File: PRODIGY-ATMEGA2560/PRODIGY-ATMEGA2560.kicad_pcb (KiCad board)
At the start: 4 copper layers, 22 parts, among them J1 DF40C-100DS-0.4V(51), J2 DF40C-100DS-0.4V(51), Q1 BC850, Q2 BC850, U1 ATmega2560-16A, U2 TXS0108EPW, U3 FT231XQ, Y1 16MHz

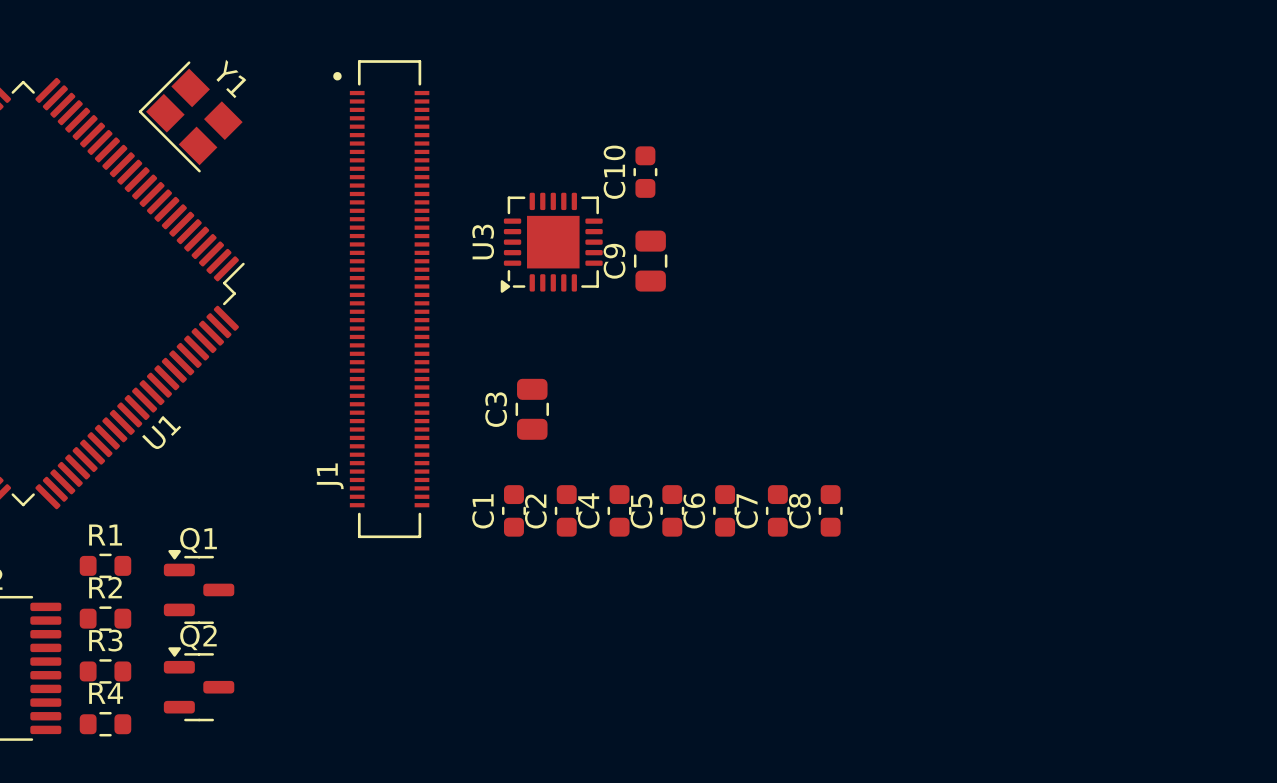
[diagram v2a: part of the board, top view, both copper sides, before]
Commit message: ESP32 and ATMEGA bom done.
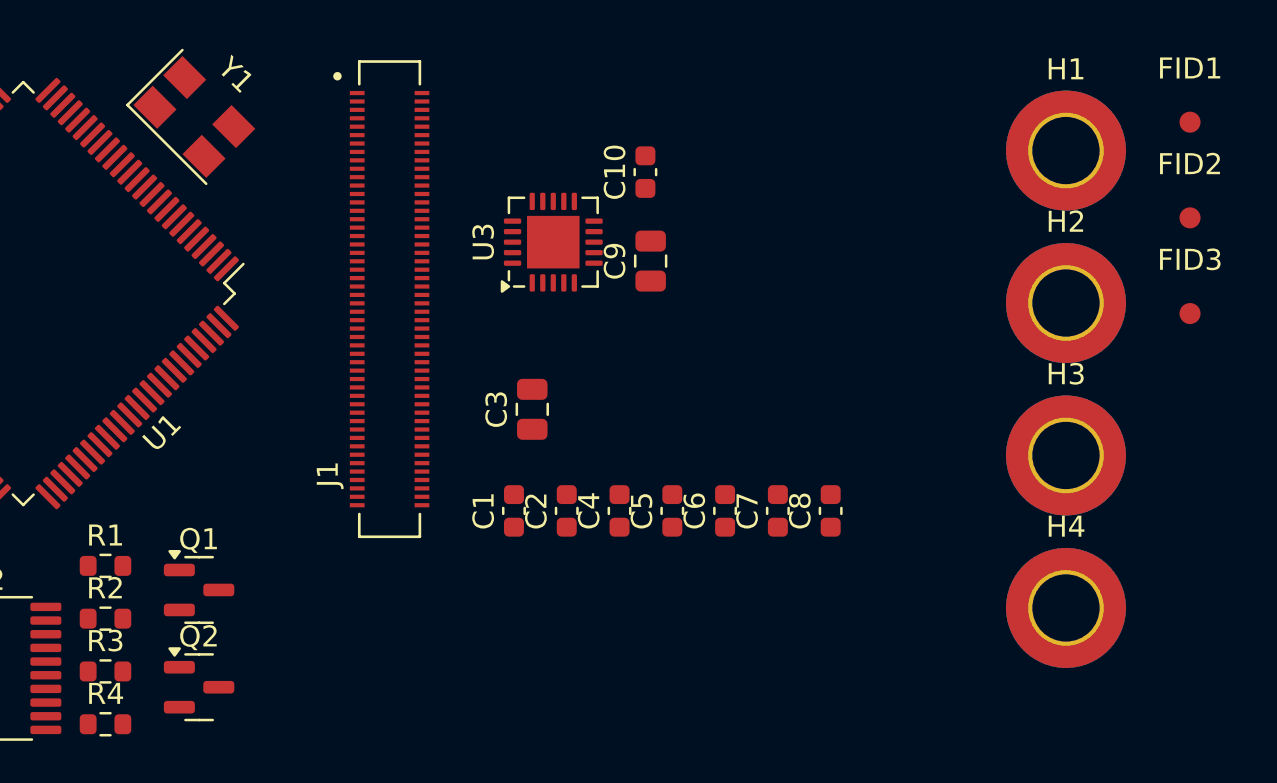
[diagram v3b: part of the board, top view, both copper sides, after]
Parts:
- added FID1: Fiducial, Fiducial:Fiducial_1mm_Mask3mm, F.Cu at (172.4, 64.9)
- added FID2: Fiducial, Fiducial:Fiducial_1mm_Mask3mm, F.Cu at (172.4, 69.5)
- added FID3: Fiducial, Fiducial:Fiducial_1mm_Mask3mm, F.Cu at (172.4, 74.0)
- added H1: MountingHole, MountingHole:MountingHole_3.2mm_M3_ISO7380_Pad_TopBottom, F.Cu at (166.5, 66.2)
- added H2: MountingHole, MountingHole:MountingHole_3.2mm_M3_ISO7380_Pad_TopBottom, F.Cu at (166.5, 73.5)
- added H3: MountingHole, MountingHole:MountingHole_3.2mm_M3_ISO7380_Pad_TopBottom, F.Cu at (166.5, 80.8)
- added H4: MountingHole, MountingHole:MountingHole_3.2mm_M3_ISO7380_Pad_TopBottom, F.Cu at (166.5, 88.0)
- C1, C2: value 10pF -> 4.7pF
- J1, J2: value DF40C-100DS-0.4V(51) -> DF40C-100DP-04V-51
- U1: value ATmega2560-16A -> ATmega2560-8A
- Y1: value 16MHz -> 8MHz; footprint Crystal:Crystal_SMD_3225-4Pin_3.2x2.5mm -> Crystal:Crystal_SMD_5032-4Pin_5.0x3.2mm

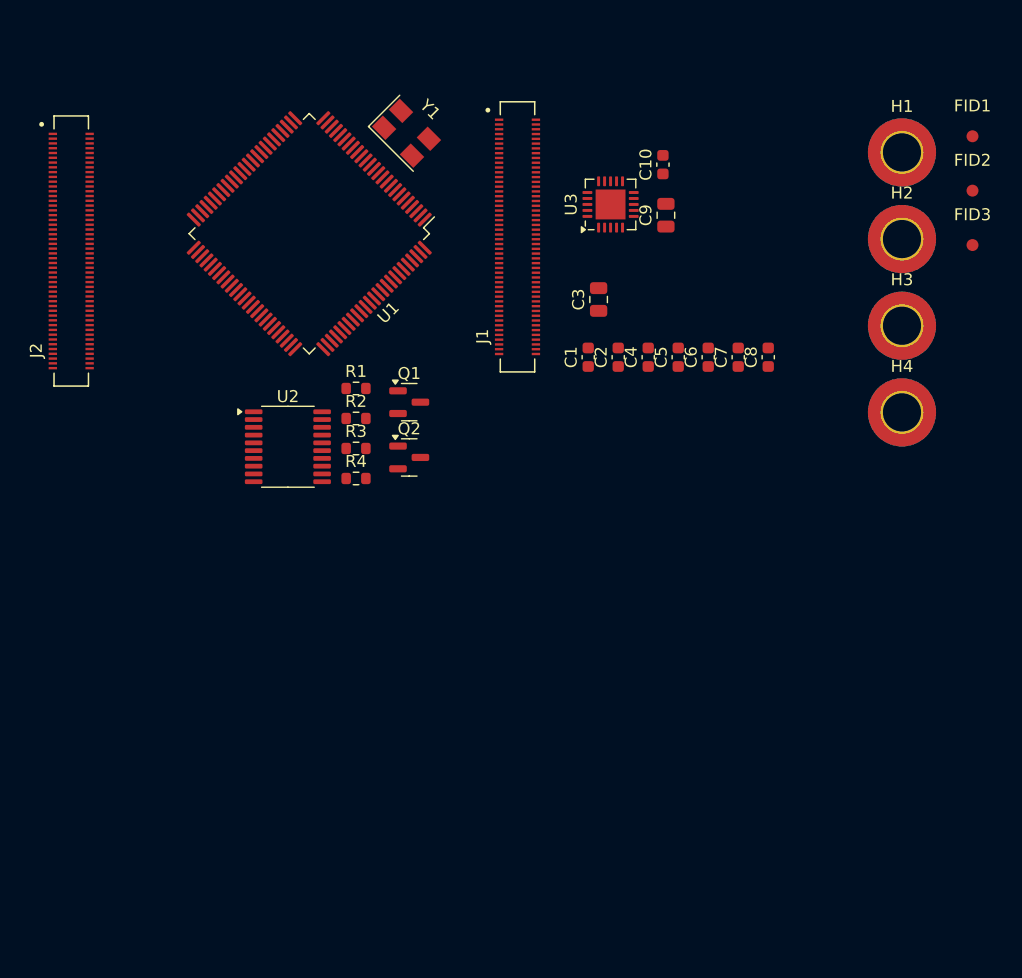
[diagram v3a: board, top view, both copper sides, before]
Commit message: Atmega layout done. orientation and alignment testing done. routing started.
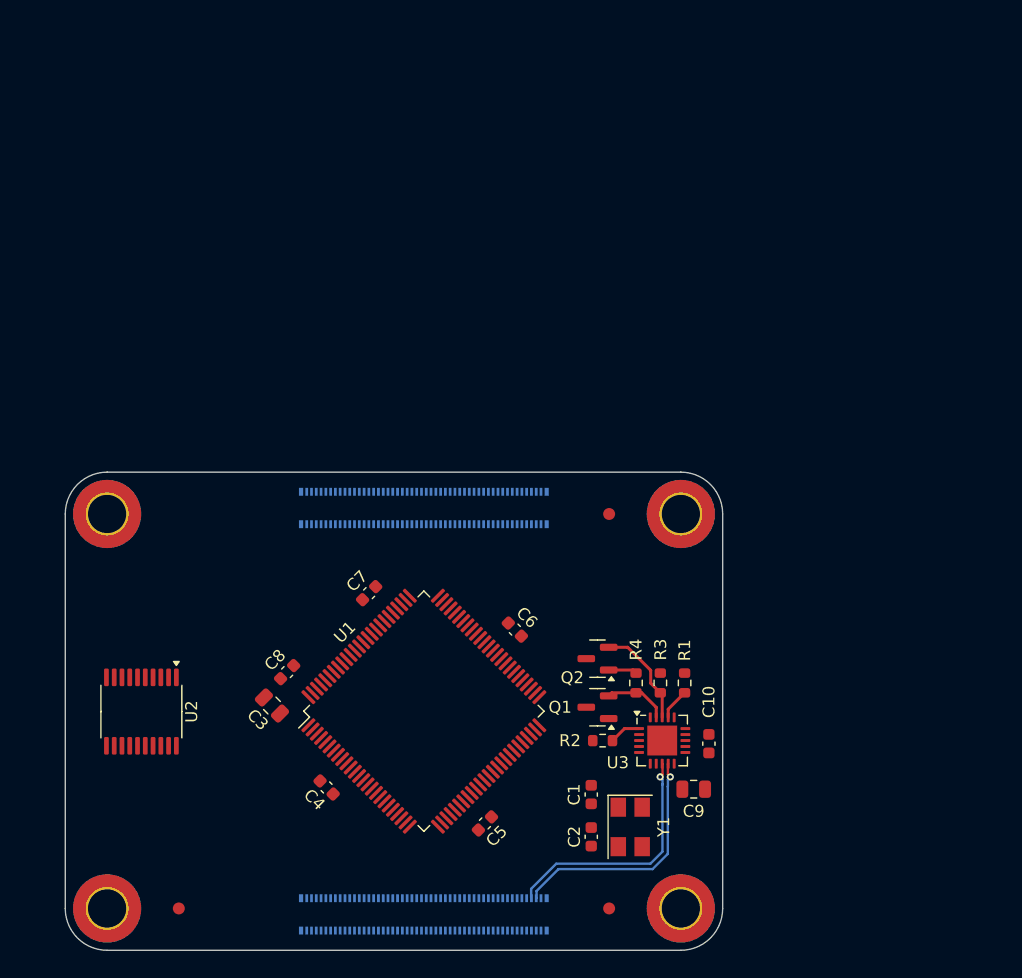
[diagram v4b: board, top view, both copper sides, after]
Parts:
- J1, J2: footprint DF40C:HIROSE_DF40C-100DS-0.4V_51_ -> DF40C-100DP-0:DF40C100DP04V51; moved to B.Cu
- moved FID2 89.5 mm to (106.0, 129.5), turned to 180 degrees
- moved H2 86.9 mm to (100.0, 129.5), turned to 180 degrees
- moved FID1 71.4 mm to (142.0, 129.5), turned to 180 degrees
- moved H3 68.3 mm to (100.0, 96.5), turned to 180 degrees
- moved H1 65.9 mm to (148.0, 129.5), turned to 180 degrees
- moved Y1 61.0 mm to (143.8, 122.7), turned to -90 degrees
- moved J1 57.2 mm to (126.5, 130.0), turned to 0 degrees
- moved C10 48.6 mm to (150.3, 115.7)
- moved C8 48.1 mm to (115.1, 109.7), turned to 45 degrees
- moved C9 48.1 mm to (149.1, 119.5), turned to 0 degrees
- moved U3 45.1 mm to (146.4, 115.5), turned to 0 degrees
- moved C4 44.9 mm to (118.4, 119.4), turned to -45 degrees
- moved C3 43.6 mm to (113.8, 112.5), turned to 135 degrees
- moved C5 42.2 mm to (131.6, 122.4), turned to 45 degrees
- moved U1 41.1 mm to (126.5, 113.0), turned to 45 degrees
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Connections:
- J1 pad 1: /connectorLeft/USB_HOST_FAULT -> /atmega2560/ANALOG_MICROPHONE
- J1 pad 10: /atmega2560/SERIAL_OUT_TX2 -> GND
- J1 pad 100: /atmega2560/ANALOG_BREAKOUT_PIEZO -> /connectorLeft/USB_HOST_ENABLE
- J1 pad 11: /atmega2560/SERIAL_OUT_TX1 -> unconnected-(J1-Pad11)
- J1 pad 12: /atmega2560/SERIAL_OUT_RX2 -> unconnected-(J1-Pad12)
- J1 pad 13: GND -> /atmega2560/ANALOG_JOYSTICK_X
- J1 pad 14: GND -> /atmega2560/ANALOG_HEATER_TEMPERATURE
- J1 pad 15: /connectorLeft/CAN_OUT_TX1 -> GND
- J1 pad 16: /connectorLeft/CAN_EN -> GND
- J1 pad 17: /connectorLeft/CAN_OUT_RX1 -> unconnected-(J1-Pad17)
- J1 pad 18: /connectorLeft/CAN_SILENT -> unconnected-(J1-Pad18)
- J1 pad 19: GND -> /atmega2560/ANALOG_PHOTOTRANSISTOR
- J1 pad 2: /connectorLeft/USB_HOST_ENABLE -> /atmega2560/ANALOG_BREAKOUT_PIEZO
- J1 pad 20: GND -> /atmega2560/ANALOG_POTENTIOMETER
- J1 pad 21: /atmega2560/I2C_SDA -> GND
- J1 pad 22: /atmega2560/MOSI -> GND
- J1 pad 23: /atmega2560/I2C_SCL -> unconnected-(J1-Pad23)
- J1 pad 24: /atmega2560/MISO -> unconnected-(J1-Pad24)
- J1 pad 25: GND -> unconnected-(J1-Pad25)
- J1 pad 26: GND -> unconnected-(J1-Pad26)
- J1 pad 27: /atmega2560/I2C_INTERRUPT_ACCEL -> GND
- J1 pad 28: /atmega2560/SCK -> GND
- J1 pad 29: /atmega2560/I2C_INTERRUPT_KEYPAD -> unconnected-(J1-Pad29)
- J1 pad 3: /connectorLeft/USB_DM -> GND
- J1 pad 30: /atmega2560/SPI_CS_BREAKOUT -> unconnected-(J1-Pad30)
- J1 pad 31: GND -> unconnected-(J1-Pad31)
- J1 pad 32: GND -> unconnected-(J1-Pad32)
- J1 pad 33: /atmega2560/DIGITAL_IR_EMITTER -> GND
- J1 pad 34: /atmega2560/SPI_CS_SEVENSEG -> GND
- J1 pad 35: /atmega2560/DIGITAL_IR_RECEIVER -> /atmega2560/MOTOR_CC_IN_1
- J1 pad 36: /atmega2560/SPI_CS_TFT -> /atmega2560/MOTOR_CC_IN_2
- J1 pad 37: GND -> /atmega2560/MOTOR_PWM_OUT_1
- J1 pad 38: GND -> /atmega2560/MOTOR_PWM_OUT_2
- J1 pad 39: /atmega2560/DIGITAL_NEOPIXEL_OUT -> GND
- J1 pad 4: /connectorLeft/USB_HOST_OUT_P- -> GND
- J1 pad 40: /atmega2560/SPI_TFT_DC -> GND
- J1 pad 41: /atmega2560/DIGITAL_RGB_R -> /atmega2560/DIGITAL_LED_OUT_1
- J1 pad 42: /atmega2560/SPI_TFT_RESET -> /atmega2560/DIGITAL_BUZZER_OUT
- J1 pad 43: /atmega2560/DIGITAL_RGB_G -> /atmega2560/DIGITAL_LED_OUT_0
- J1 pad 44: GND -> /atmega2560/DIGITAL_LED_OUT_2
- J1 pad 45: /atmega2560/DIGITAL_RGB_B -> GND
- J1 pad 46: /atmega2560/SPI_CS_NFC -> GND
- J1 pad 47: /atmega2560/DIGITAL_BUTTON_IN_0 -> /atmega2560/DIGITAL_BUTTON_IN_3
- J1 pad 48: /atmega2560/SPI_IRQ_NFC -> /atmega2560/DIGITAL_HEATER_OUT
- J1 pad 49: /atmega2560/DIGITAL_BUTTON_IN_1 -> /atmega2560/DIGITAL_BUTTON_IN_2
- J1 pad 5: /connectorLeft/USB_DP -> unconnected-(J1-Pad5)
- J1 pad 50: GND -> /atmega2560/SPI_RST_NFC
- J1 pad 51: /atmega2560/DIGITAL_BUTTON_IN_2 -> /atmega2560/DIGITAL_BUTTON_IN_1
- J1 pad 52: /atmega2560/SPI_RST_NFC -> GND
- J1 pad 53: /atmega2560/DIGITAL_BUTTON_IN_3 -> /atmega2560/DIGITAL_BUTTON_IN_0
- J1 pad 54: /atmega2560/DIGITAL_HEATER_OUT -> /atmega2560/SPI_IRQ_NFC
- J1 pad 55: GND -> /atmega2560/DIGITAL_RGB_B
- J1 pad 56: GND -> /atmega2560/SPI_CS_NFC
- J1 pad 57: /atmega2560/DIGITAL_LED_OUT_0 -> /atmega2560/DIGITAL_RGB_G
- J1 pad 58: /atmega2560/DIGITAL_LED_OUT_2 -> GND
- J1 pad 59: /atmega2560/DIGITAL_LED_OUT_1 -> /atmega2560/DIGITAL_RGB_R
- J1 pad 6: /connectorLeft/USB_HOST_OUT_P+ -> unconnected-(J1-Pad6)
- J1 pad 60: /atmega2560/DIGITAL_BUZZER_OUT -> /atmega2560/SPI_TFT_RESET
- J1 pad 61: GND -> /atmega2560/DIGITAL_NEOPIXEL_OUT
- J1 pad 62: GND -> /atmega2560/SPI_TFT_DC
- J1 pad 63: /atmega2560/MOTOR_PWM_OUT_1 -> GND
- J1 pad 64: /atmega2560/MOTOR_PWM_OUT_2 -> GND
- J1 pad 65: /atmega2560/MOTOR_CC_IN_1 -> /atmega2560/DIGITAL_IR_RECEIVER
- J1 pad 66: /atmega2560/MOTOR_CC_IN_2 -> /atmega2560/SPI_CS_TFT
- J1 pad 67: GND -> /atmega2560/DIGITAL_IR_EMITTER
- J1 pad 68: GND -> /atmega2560/SPI_CS_SEVENSEG
- J1 pad 69: unconnected-(J1-Pad69) -> GND
- J1 pad 7: GND -> /atmega2560/ANALOG_JOYSTICK_Y
- J1 pad 70: unconnected-(J1-Pad70) -> GND
- J1 pad 71: unconnected-(J1-Pad71) -> /atmega2560/I2C_INTERRUPT_KEYPAD
- J1 pad 72: unconnected-(J1-Pad72) -> /atmega2560/SPI_CS_BREAKOUT
- J1 pad 73: GND -> /atmega2560/I2C_INTERRUPT_ACCEL
- J1 pad 74: GND -> /atmega2560/SCK
- J1 pad 75: unconnected-(J1-Pad75) -> GND
- J1 pad 76: unconnected-(J1-Pad76) -> GND
- J1 pad 77: unconnected-(J1-Pad77) -> /atmega2560/I2C_SCL
- J1 pad 78: unconnected-(J1-Pad78) -> /atmega2560/MISO
- J1 pad 79: GND -> /atmega2560/I2C_SDA
- J1 pad 8: GND -> /atmega2560/ANALOG_BREAKOUT_PT100
- J1 pad 80: GND -> /atmega2560/MOSI
- J1 pad 81: /atmega2560/ANALOG_PHOTOTRANSISTOR -> GND
- J1 pad 82: /atmega2560/ANALOG_POTENTIOMETER -> GND
- J1 pad 83: unconnected-(J1-Pad83) -> /connectorLeft/CAN_OUT_RX1
- J1 pad 84: unconnected-(J1-Pad84) -> /connectorLeft/CAN_SILENT
- J1 pad 85: GND -> /connectorLeft/CAN_OUT_TX1
- J1 pad 86: GND -> /connectorLeft/CAN_EN
- J1 pad 87: /atmega2560/ANALOG_JOYSTICK_X -> GND
- J1 pad 88: /atmega2560/ANALOG_HEATER_TEMPERATURE -> GND
- J1 pad 89: unconnected-(J1-Pad89) -> /atmega2560/SERIAL_OUT_TX1
- J1 pad 9: /atmega2560/SERIAL_OUT_RX1 -> GND
- J1 pad 90: unconnected-(J1-Pad90) -> /atmega2560/SERIAL_OUT_RX2
- J1 pad 91: GND -> /atmega2560/SERIAL_OUT_RX1
- J1 pad 92: GND -> /atmega2560/SERIAL_OUT_TX2
- J1 pad 93: /atmega2560/ANALOG_JOYSTICK_Y -> GND
- J1 pad 94: /atmega2560/ANALOG_BREAKOUT_PT100 -> GND
- J1 pad 95: unconnected-(J1-Pad95) -> /connectorLeft/USB+
- J1 pad 96: unconnected-(J1-Pad96) -> /connectorLeft/USB_HOST_OUT_P+
- J1 pad 97: GND -> /connectorLeft/USB-
- J1 pad 98: GND -> /connectorLeft/USB_HOST_OUT_P-
- J1 pad 99: /atmega2560/ANALOG_MICROPHONE -> /connectorLeft/USB_HOST_FAULT
- J2 pad 1: GND -> unconnected-(J2-Pad1)
- J2 pad 100: /atmega2560/MCU_RESET -> GND
- J2 pad 12: unconnected-(J2-Pad12) -> +3V3
- J2 pad 13: GND -> +5V
- J2 pad 14: GND -> +3V3
- J2 pad 15: unconnected-(J2-Pad15) -> +5V
- J2 pad 16: unconnected-(J2-Pad16) -> +3V3
- J2 pad 17: unconnected-(J2-Pad17) -> +5V
- J2 pad 18: unconnected-(J2-Pad18) -> +3V3
- J2 pad 19: unconnected-(J2-Pad19) -> +5V
- J2 pad 2: GND -> /atmega2560/MCU_RESET
- J2 pad 21: unconnected-(J2-Pad21) -> +5V
- J2 pad 22: GND -> unconnected-(J2-Pad22)
- J2 pad 23: GND -> +5V
- J2 pad 24: /atmega2560/MCU_GPIO_26 -> /connectorRight/MCU_VREF
- J2 pad 25: /atmega2560/MCU_GPIO_21 -> /atmega2560/SD_Enable
- J2 pad 26: /atmega2560/MCU_GPIO_19 -> /atmega2560/SD_DET
- J2 pad 27: /atmega2560/MCU_GPIO_20 -> unconnected-(J2-Pad27)
- J2 pad 28: /atmega2560/MCU_GPIO_13 -> GND
- J2 pad 29: /atmega2560/MCU_GPIO_16 -> GND
- J2 pad 30: /atmega2560/MCU_GPIO_6 -> unconnected-(J2-Pad30)
- J2 pad 31: /atmega2560/MCU_GPIO_12 -> /atmega2560/SD_DAT2
- J2 pad 32: GND -> unconnected-(J2-Pad32)
- J2 pad 33: GND -> /atmega2560/SD_DAT0
- J2 pad 34: /atmega2560/MCU_GPIO_5 -> unconnected-(J2-Pad34)
- J2 pad 35: unconnected-(J2-Pad35) -> GND
- J2 pad 36: unconnected-(J2-Pad36) -> GND
- J2 pad 37: /atmega2560/MCU_GPIO_7 -> /atmega2560/SD_DAT1
- J2 pad 38: /atmega2560/MCU_GPIO_11 -> unconnected-(J2-Pad38)
- J2 pad 39: /atmega2560/MCU_GPIO_8 -> /atmega2560/SD_DAT3
- J2 pad 4: unconnected-(J2-Pad4) -> GND
- J2 pad 40: /atmega2560/MCU_GPIO_9 -> /atmega2560/SD_CMD
- J2 pad 41: /atmega2560/MCU_GPIO_25 -> GND
- J2 pad 43: GND -> /atmega2560/SD_CLK
- J2 pad 44: /atmega2560/MCU_GPIO_10 -> /atmega2560/MCU_GPIO_2
- J2 pad 45: /atmega2560/MCU_GPIO_24 -> /atmega2560/MCU_GPIO_14
- J2 pad 46: /atmega2560/MCU_GPIO_22 -> /atmega2560/MCU_GPIO_3
- J2 pad 47: /atmega2560/MCU_GPIO_23 -> GND
- J2 pad 48: /atmega2560/MCU_GPIO_27 -> /atmega2560/MCU_GPIO_4
- J2 pad 49: /atmega2560/MCU_GPIO_18 -> /atmega2560/MCU_GPIO_15
- J2 pad 50: /atmega2560/MCU_GPIO_17 -> GND
- J2 pad 51: /atmega2560/MCU_GPIO_15 -> /atmega2560/MCU_GPIO_18
- J2 pad 52: GND -> /atmega2560/MCU_GPIO_17
- J2 pad 53: GND -> /atmega2560/MCU_GPIO_23
- J2 pad 54: /atmega2560/MCU_GPIO_4 -> /atmega2560/MCU_GPIO_27
- J2 pad 55: /atmega2560/MCU_GPIO_14 -> /atmega2560/MCU_GPIO_24
- J2 pad 56: /atmega2560/MCU_GPIO_3 -> /atmega2560/MCU_GPIO_22
- J2 pad 57: /atmega2560/SD_CLK -> GND
- J2 pad 58: /atmega2560/MCU_GPIO_2 -> /atmega2560/MCU_GPIO_10
- J2 pad 59: GND -> /atmega2560/MCU_GPIO_25
- J2 pad 61: /atmega2560/SD_DAT3 -> /atmega2560/MCU_GPIO_8
- J2 pad 62: /atmega2560/SD_CMD -> /atmega2560/MCU_GPIO_9
- J2 pad 63: /atmega2560/SD_DAT1 -> /atmega2560/MCU_GPIO_7
- J2 pad 64: unconnected-(J2-Pad64) -> /atmega2560/MCU_GPIO_11
- J2 pad 65: GND -> unconnected-(J2-Pad65)
- J2 pad 66: GND -> unconnected-(J2-Pad66)
- J2 pad 67: /atmega2560/SD_DAT0 -> GND
- J2 pad 68: unconnected-(J2-Pad68) -> /atmega2560/MCU_GPIO_5
- J2 pad 69: /atmega2560/SD_DAT2 -> /atmega2560/MCU_GPIO_12
- J2 pad 7: GND -> unconnected-(J2-Pad7)
- J2 pad 70: unconnected-(J2-Pad70) -> GND
- J2 pad 71: GND -> /atmega2560/MCU_GPIO_16
- J2 pad 72: unconnected-(J2-Pad72) -> /atmega2560/MCU_GPIO_6
- J2 pad 73: unconnected-(J2-Pad73) -> /atmega2560/MCU_GPIO_20
- J2 pad 74: GND -> /atmega2560/MCU_GPIO_13
- J2 pad 75: /atmega2560/SD_Enable -> /atmega2560/MCU_GPIO_21
- J2 pad 76: /atmega2560/SD_DET -> /atmega2560/MCU_GPIO_19
- J2 pad 77: +5V -> GND
- J2 pad 78: /connectorRight/MCU_VREF -> /atmega2560/MCU_GPIO_26
- J2 pad 79: +5V -> unconnected-(J2-Pad79)
- J2 pad 8: GND -> unconnected-(J2-Pad8)
- J2 pad 80: unconnected-(J2-Pad80) -> GND
- J2 pad 81: +5V -> unconnected-(J2-Pad81)
- J2 pad 83: +5V -> unconnected-(J2-Pad83)
- J2 pad 84: +3V3 -> unconnected-(J2-Pad84)
- J2 pad 85: +5V -> unconnected-(J2-Pad85)
- J2 pad 86: +3V3 -> unconnected-(J2-Pad86)
- J2 pad 87: +5V -> GND
- J2 pad 88: +3V3 -> GND
- J2 pad 90: +3V3 -> unconnected-(J2-Pad90)
- J2 pad 93: unconnected-(J2-Pad93) -> GND
- J2 pad 94: unconnected-(J2-Pad94) -> GND
- J2 pad 98: GND -> unconnected-(J2-Pad98)
- J2 pad 99: unconnected-(J2-Pad99) -> GND
- U2 pad 10: +3.3V -> +3V3
- U2 pad 2: +3.3V -> +3V3
- U3 pad 8: /connectorLeft/USB_DP -> /connectorLeft/USB+
- U3 pad 9: /connectorLeft/USB_DM -> /connectorLeft/USB-
- Y1 pad 1: Net-(U1-XTAL2) -> Net-(U1-XTAL1)
- Y1 pad 2: Net-(U1-XTAL1) -> GND
- Y1 pad 3: (no net) -> Net-(U1-XTAL2)
- Y1 pad 4: (no net) -> GND
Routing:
- net /connectorLeft/USB+: track 0.00 -> 20.6 mm, vias 0 -> 1
- net /connectorLeft/USB-: track 0.00 -> 20.6 mm, vias 0 -> 1
- net /usbBridge/DTR: track 0.00 -> 8.65 mm
- net /usbBridge/RTS: track 0.00 -> 5.43 mm
- net Net-(U3-RXD): track 0.00 -> 2.64 mm
- net Net-(U3-TXD): track 0.00 -> 2.62 mm
- net Net-(Q2-B): track 0.00 -> 2.39 mm
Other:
- board outline added: 55 x 40 mm

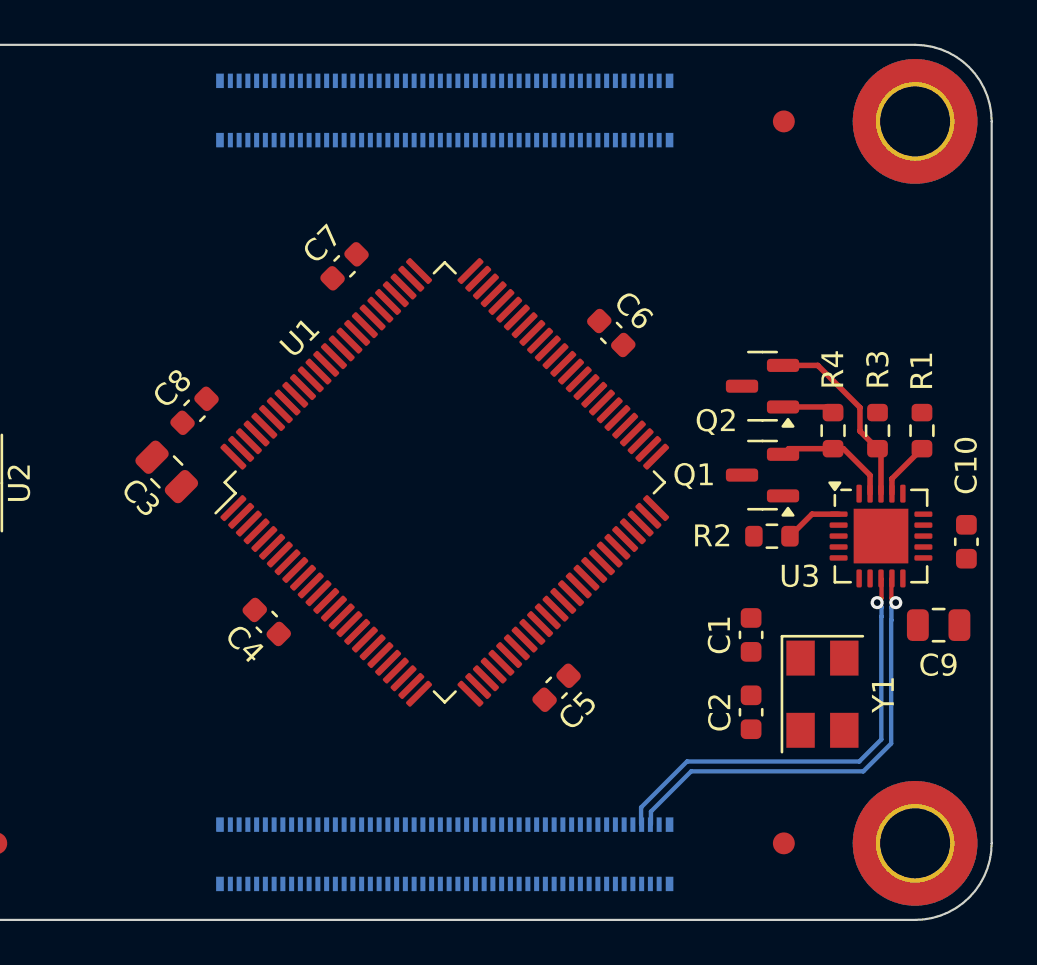
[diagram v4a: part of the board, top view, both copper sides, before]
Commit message: vias done, some routing done. analog routing done
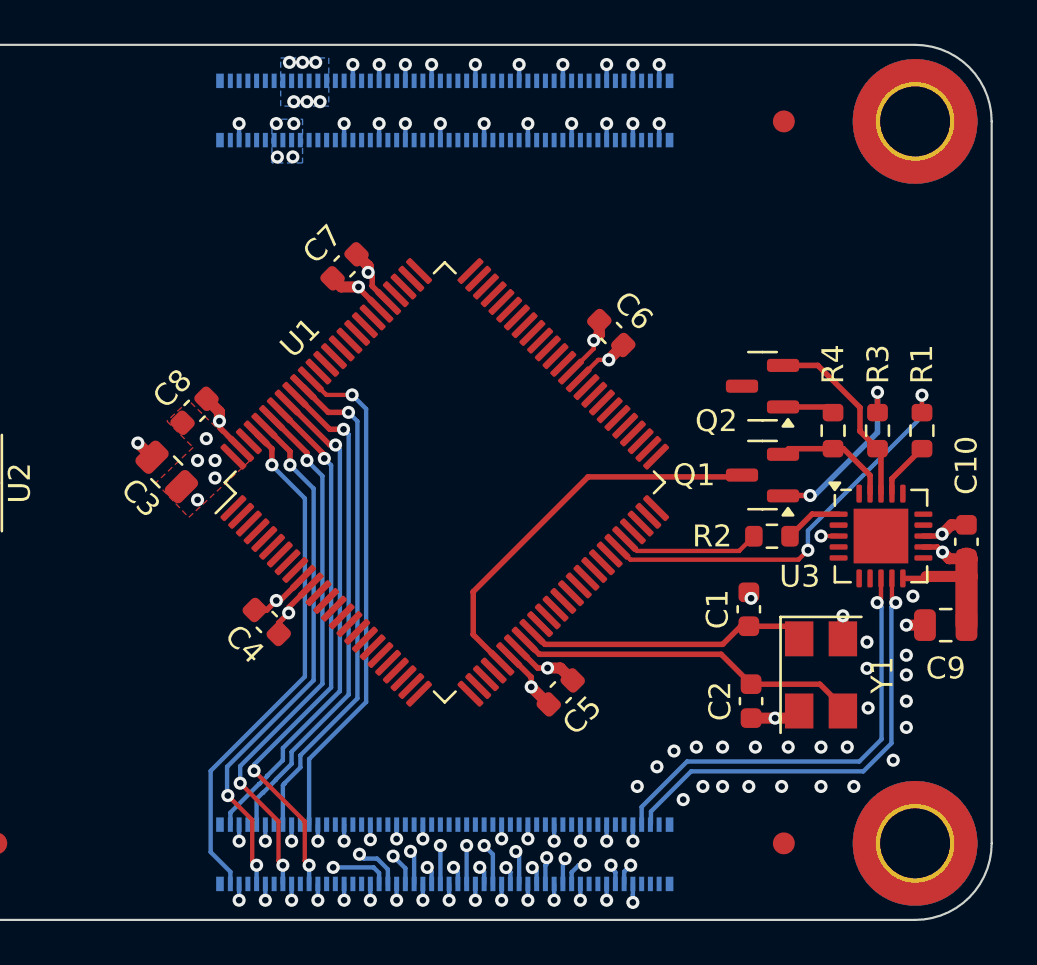
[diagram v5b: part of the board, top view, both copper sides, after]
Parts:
- moved C1 1.18 mm to (140.4, 118.8)
- moved Y1 0.88 mm to (143.7, 121.8)
- moved C2 0.51 mm to (140.5, 123.0)
- moved C9 0.32 mm to (149.4, 119.5), turned to 180 degrees
- moved C5 0.28 mm to (131.8, 122.6)
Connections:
- U1 pad 24: /atmega2560/DIGITAL_RGB_R -> /atmega2560/DIGITAL_RGB_B
- U1 pad 26: /atmega2560/DIGITAL_RGB_B -> /atmega2560/DIGITAL_RGB_R
- U1 pad 90: /atmega2560/ANALOG_BREAKOUT_PIEZO -> /atmega2560/ANALOG_PHOTOTRANSISTOR
- U1 pad 91: /atmega2560/ANALOG_BREAKOUT_PT100 -> /atmega2560/ANALOG_JOYSTICK_X
- U1 pad 92: /atmega2560/ANALOG_MICROPHONE -> /atmega2560/ANALOG_JOYSTICK_Y
- U1 pad 93: /atmega2560/ANALOG_JOYSTICK_Y -> /atmega2560/ANALOG_MICROPHONE
- U1 pad 94: /atmega2560/ANALOG_JOYSTICK_X -> /atmega2560/ANALOG_POTENTIOMETER
- U1 pad 95: /atmega2560/ANALOG_PHOTOTRANSISTOR -> /atmega2560/ANALOG_HEATER_TEMPERATURE
- U1 pad 96: /atmega2560/ANALOG_HEATER_TEMPERATURE -> /atmega2560/ANALOG_BREAKOUT_PT100
- U1 pad 97: /atmega2560/ANALOG_POTENTIOMETER -> /atmega2560/ANALOG_BREAKOUT_PIEZO
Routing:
- net GND: track 0.00 -> 60.9 mm, vias 0 -> 88
- net /atmega2560/ANALOG_POTENTIOMETER: track 0.00 -> 25.1 mm, vias 0 -> 3
- net /atmega2560/ANALOG_HEATER_TEMPERATURE: track 0.00 -> 24.6 mm, vias 0 -> 3
- net /atmega2560/ANALOG_BREAKOUT_PIEZO: track 0.00 -> 24.2 mm, vias 0 -> 1
- net /atmega2560/ANALOG_BREAKOUT_PT100: track 0.00 -> 24.2 mm, vias 0 -> 3
- net /atmega2560/ANALOG_JOYSTICK_X: track 0.00 -> 23.7 mm, vias 0 -> 1
- net /atmega2560/ANALOG_PHOTOTRANSISTOR: track 0.00 -> 23.2 mm, vias 0 -> 1
- net /atmega2560/ANALOG_JOYSTICK_Y: track 0.00 -> 22.8 mm, vias 0 -> 1
- net /atmega2560/ANALOG_MICROPHONE: track 0.00 -> 22.5 mm, vias 0 -> 1
- net +5V: track 0.00 -> 19.5 mm, vias 0 -> 16
- net /atmega2560/USB_RX: track 0.00 -> 19.2 mm, vias 0 -> 2
- net /atmega2560/MCU_RESET: track 0.00 -> 18.3 mm
- net Net-(U1-XTAL2): track 0.13 -> 16.0 mm
- net Net-(U1-XTAL1): track 0.40 -> 13.0 mm
- net Net-(Q1-B): track 0.00 -> 8.28 mm, vias 0 -> 2
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- added copper zone on B.Cu, net +3V3
- added copper zone on B.Cu, net +5V
- added copper zone on F.Cu, net +5V
- added copper zone on In2.Cu, net GND
